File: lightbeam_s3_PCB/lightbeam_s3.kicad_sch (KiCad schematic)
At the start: 70 parts, among them J1 USB4105-GF-A, J2 uFL, J3 Conn_01x08_Socket, J4 JST-SM04B-SRSS, J5 JST-SM04B-SRSS, J6 JST-SM04B-SRSS, SW1 PTS636 SK25F, SW2 PTS636 SK25F, U1 ESP32-S3-WROOM-2-N32R8V, U2 AP2112K-3.3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

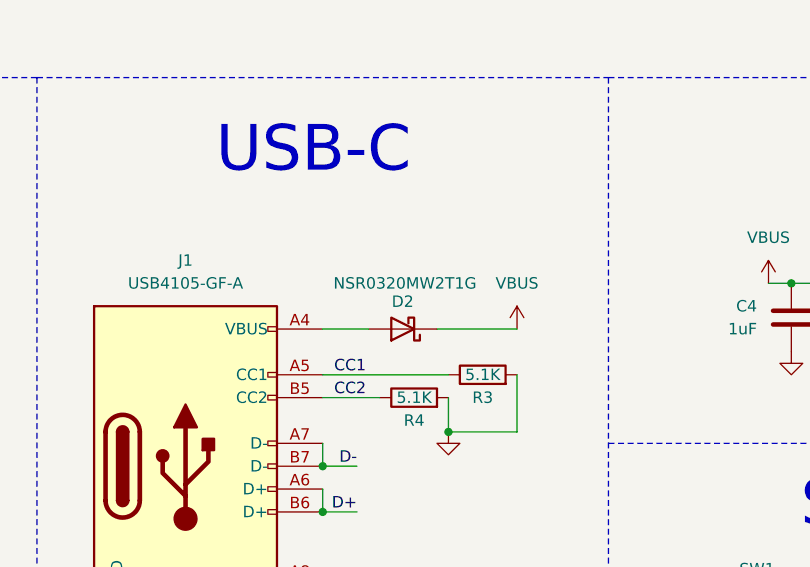
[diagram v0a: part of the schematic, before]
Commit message: Increase diode to 2A
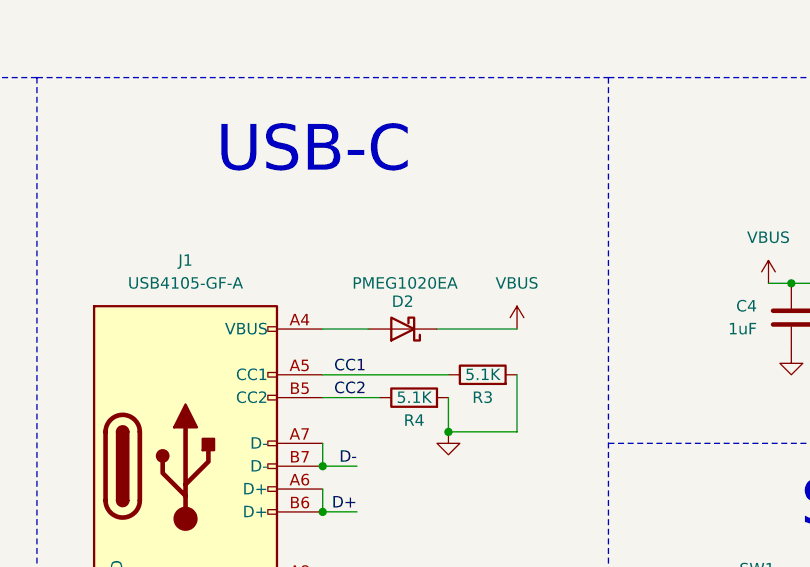
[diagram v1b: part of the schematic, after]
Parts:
- D2: value NSR0320MW2T1G -> PMEG1020EA
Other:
- title: Binary Neopixel Clock -> Lightbeam S3

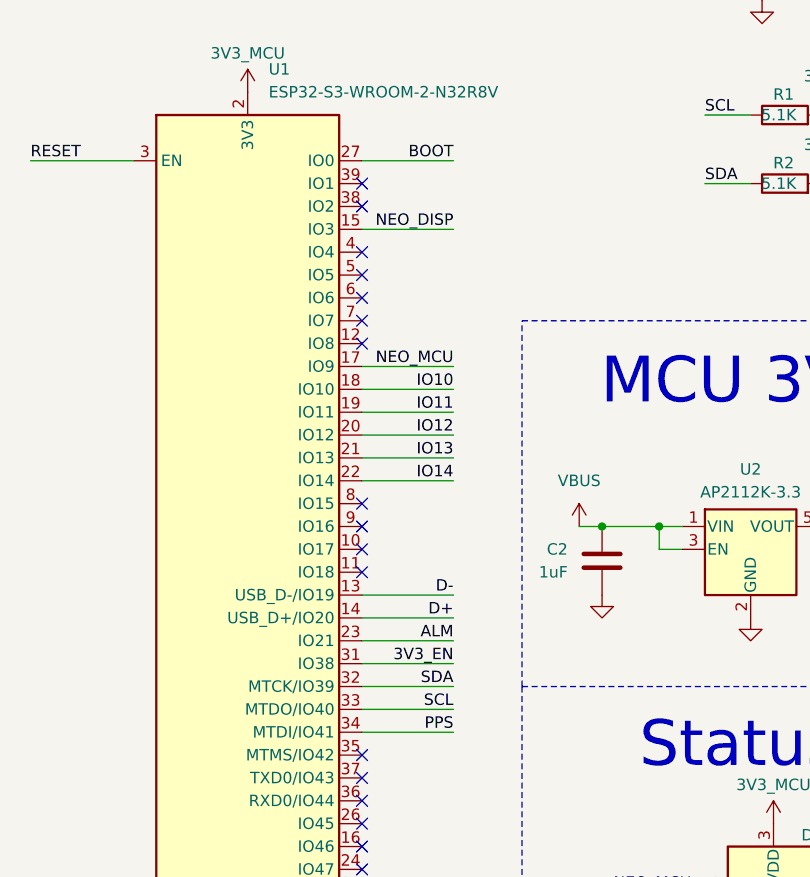
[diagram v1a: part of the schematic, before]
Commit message: Fix I2C lines, remove edge power line
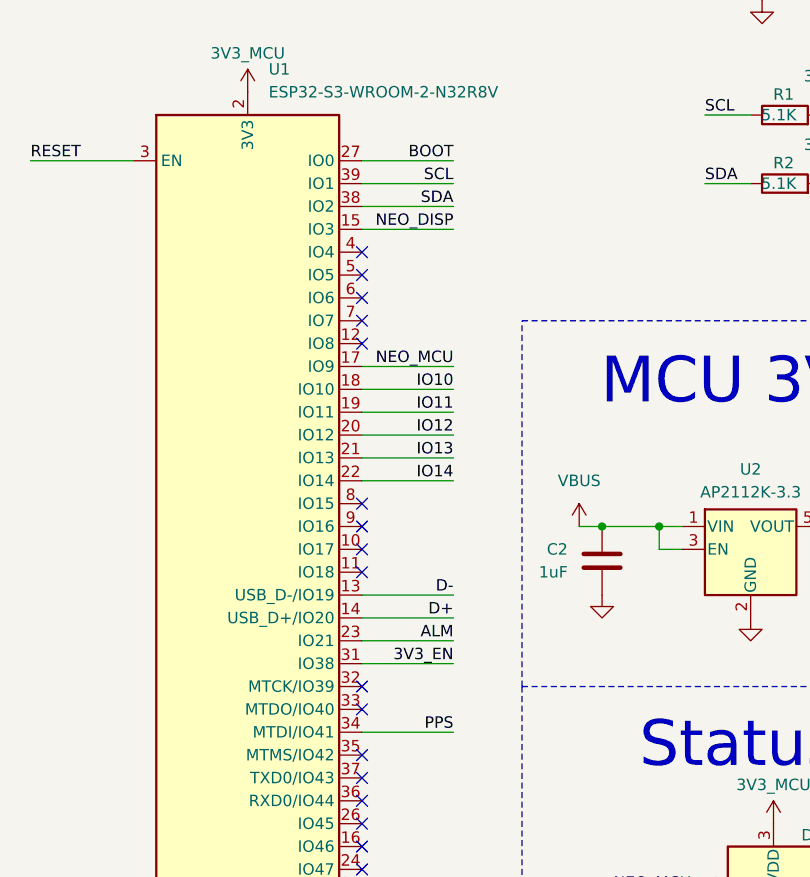
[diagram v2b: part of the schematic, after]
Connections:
- net SCL: now also U1.39 (IO1); no longer U1.33 (MTDO/IO40)
- net SDA: now also U1.38 (IO2); no longer U1.32 (MTCK/IO39)
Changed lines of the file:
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@@
+	)
+	(no_connect
+		(at 53.34 250.19)
 	)
 	(no_connect
@@
 	)
 	(no_connect
+		(at 53.34 252.73)
+	)
+	(no_connect
 		(at 171.45 254)
 	)
@@
 	)
 	(no_connect
+		(at 53.34 234.95)
+	)
+	(no_connect
+		(at 53.34 260.35)
+	)
+	(no_connect
+		(at 212.09 266.7)
+	)
+	(no_connect
+		(at 148.59 204.47)
+	)
+	(no_connect
+		(at 140.97 251.46)
+	)
+	(no_connect
+		(at 53.34 237.49)
+	)
+	(no_connect
+		(at 53.34 212.09)
+	)
+	(no_connect
+		(at 156.21 241.3)
+	)
+	(no_connect
+		(at 53.34 204.47)
+	)
+	(no_connect
+		(at 53.34 265.43)
+	)
+	(no_connect
+		(at 53.34 257.81)
+	)
+	(no_connect
 		(at 53.34 270.51)
 	)
 	(no_connect
-		(at 53.34 234.95)
-	)
-	(no_connect
-		(at 53.34 260.35)
-	)
-	(no_connect
-		(at 53.34 194.31)
-	)
-	(no_connect
-		(at 212.09 266.7)
-	)
-	(no_connect
-		(at 148.59 204.47)
-	)
-	(no_connect
-		(at 140.97 251.46)
-	)
-	(no_connect
-		(at 53.34 237.49)
-	)
-	(no_connect
-		(at 53.34 212.09)
-	)
-	(no_connect
-		(at 156.21 241.3)
-	)
-	(no_connect
-		(at 53.34 204.47)
-	)
-	(no_connect
-		(at 53.34 265.43)
-	)
-	(no_connect
-		(at 53.34 257.81)
-	)
-	(no_connect
 		(at 148.59 207.01)
 	)
 	(no_connect
-		(at 53.34 196.85)
-	)
-	(no_connect
 		(at 53.34 262.89)
 	)
@@
 	(wire
 		(pts
+			(xy 53.34 196.85) (xy 63.5 196.85)
+		)
+		(stroke
+			(width 0)
+			(type default)
+		)
+	)
+	(wire
+		(pts
 			(xy 374.65 205.74) (xy 375.92 205.74)
 		)
@@
 	(wire
 		(pts
+			(xy 53.34 194.31) (xy 63.5 194.31)
+		)
+		(stroke
+			(width 0)
+			(type default)
+		)
+	)
+	(wire
+		(pts
 			(xy 204.47 43.18) (xy 223.52 43.18)
 		)
@@
 	(wire
 		(pts
-			(xy 53.34 250.19) (xy 63.5 250.19)
-		)
-		(stroke
-			(width 0)
-			(type default)
-		)
-	)
-	(wire
-		(pts
 			(xy 223.52 247.65) (xy 222.25 247.65)
 		)
@@
 		(pts
 			(xy 203.2 173.99) (xy 209.55 173.99)
-		)
-		(stroke
-			(width 0)
-			(type default)
-		)
-	)
-	(wire
-		(pts
-			(xy 53.34 252.73) (xy 63.5 252.73)
 		)
 		(stroke
@@
 	)
 	(label "SCL"
+		(at 63.5 194.31 180)
+		(fields_autoplaced yes)
+		(effects
+			(font
+				(size 1.27 1.27)
+			)
+			(justify right bottom)
+		)
+	)
+	(label "SCL"
 		(at 203.2 256.54 0)
 		(fields_autoplaced yes)
@@
 		)
 	)
-	(label "SCL"
-		(at 63.5 252.73 180)
-		(fields_autoplaced yes)
-		(effects
-			(font
-				(size 1.27 1.27)
-			)
-			(justify right bottom)
-		)
-	)
 	(label "RSR_SCL"
 		(at 302.26 208.28 0)
@@
 		)
 	)
+	(label "SDA"
+		(at 63.5 196.85 180)
+		(fields_autoplaced yes)
+		(effects
+			(font
+				(size 1.27 1.27)
+			)
+			(justify right bottom)
+		)
+	)
 	(label "D-"
 		(at 152.4 191.77 180)
 		(fields_autoplaced yes)
 		(effects
-			(font
-				(size 1.27 1.27)
-			)
-			(justify right bottom)
-		)
-	)
-	(label "SDA"
-		(at 63.5 250.19 180)
-		(fields_autoplaced yes)
-		(effects

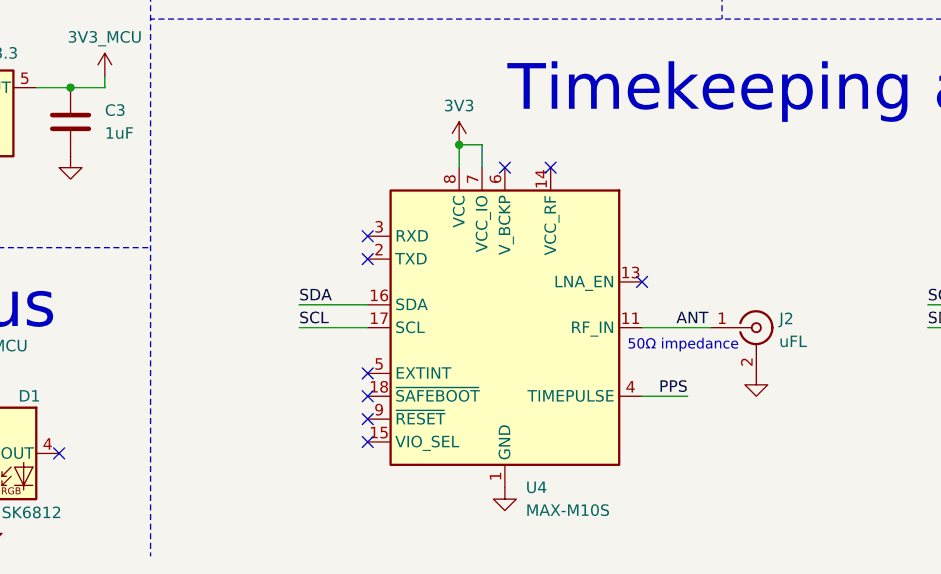
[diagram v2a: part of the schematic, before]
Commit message: DNP GNSS module
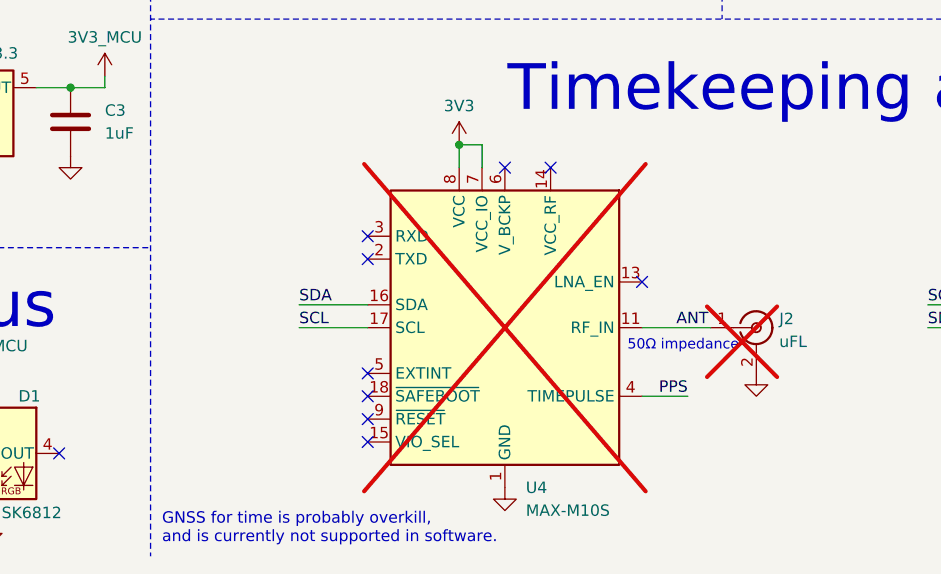
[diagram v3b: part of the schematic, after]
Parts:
- J2, U4: now not fitted
- U8: now left out of the parts list
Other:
- note added: "GNSS for time is probably overkill, and is currently not supported in software."
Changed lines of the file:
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@@
 		)
 	)
+	(text "GNSS for time is probably overkill, \nand is currently not supported in software."
+		(exclude_from_sim no)
+		(at 118.11 281.432 0)
+		(effects
+			(font
+				(size 1.27 1.27)
+			)
+			(justify left)
+		)
+	)
 	(text "Timekeeping and Light Sensor\n"
 		(exclude_from_sim no)
@@
 		(in_bom yes)
 		(on_board yes)
-		(dnp no)
+		(dnp yes)
 		(fields_autoplaced yes)
 		(property "Reference" "U4"
@@
 		(unit 1)
 		(exclude_from_sim no)
-		(in_bom yes)
-		(on_board yes)
+		(in_bom no)
+		(on_board no)
 		(dnp yes)
 		(property "Reference" "U8"
@@
 		(in_bom yes)
 		(on_board yes)
-		(dnp no)
+		(dnp yes)
 		(fields_autoplaced yes)
 		(property "Reference" "J2"

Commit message: Improve PCB for the enclosure, clean traces, DNP GNSS
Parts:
- C28: now not fitted; now left out of the parts list
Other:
- note added: "In case of dim environments, the sensor can be on a daughterboard for better light visibility where it sticks out more from the enlcosure. It is attached with a Qwiic connecter (JST-SH with I2C). This is to save cost from it being a seperate PCB."
- note removed: "In case the normal position of the light sensor is sheilded by the case, this part of the PCB can be removed so the light sensor can be on a daughterboard for better light visibility. It is attached with a Qwiic connecter (JST-SH with I2C). This is to save cost from it being a seperate PCB."
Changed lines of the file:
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@@
 		)
 	)
-	(text "In case the normal position of the light sensor is sheilded \nby the case, this part of the PCB can be removed so the light\nsensor can be on a daughterboard for better light visibility. \nIt is attached with a Qwiic connecter (JST-SH with I2C).\nThis is to save cost from it being a seperate PCB.\n"
+	(text "In case of dim environments, the sensor can be on \na daughterboard for better light visibility where \nit sticks out more from the enlcosure. It is \nattached with a Qwiic connecter (JST-SH with I2C).\nThis is to save cost from it being a seperate PCB.\n"
 		(exclude_from_sim no)
-		(at 359.41 247.142 0)
+		(at 343.662 238.252 0)
 		(effects
 			(font
-				(size 1.27 1.27)
+				(size 1.651 1.651)
 			)
 			(justify left)
@@
 	(text "GNSS for time is probably overkill, \nand is currently not supported in software."
 		(exclude_from_sim no)
-		(at 118.11 281.432 0)
+		(at 117.348 281.432 0)
 		(effects
 			(font
-				(size 1.27 1.27)
+				(size 1.651 1.651)
 			)
 			(justify left)
@@
 		(exclude_from_sim no)
 		(in_bom no)
-		(on_board yes)
+		(on_board no)
 		(dnp yes)
 		(property "Reference" "J5"
@@
 		(unit 1)
 		(exclude_from_sim no)
-		(in_bom yes)
-		(on_board yes)
-		(dnp no)
+		(in_bom no)
+		(on_board no)
+		(dnp yes)
 		(property "Reference" "C28"
 			(at 378.714 213.36 0)
@@
 		(exclude_from_sim no)
 		(in_bom no)
-		(on_board yes)
+		(on_board no)
 		(dnp yes)
 		(property "Reference" "J6"
